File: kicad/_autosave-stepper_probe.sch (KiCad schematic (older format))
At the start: 49 parts, among them J1 Conn_01x04_Male, J2 Conn_01x04_Male, J3 BAT, J4 Serial Port, J5 SWD, J6 Reset header, M1 Motor, Q1 PJA3439, SW1 SW_Push, U1 CC6920BSO-5A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

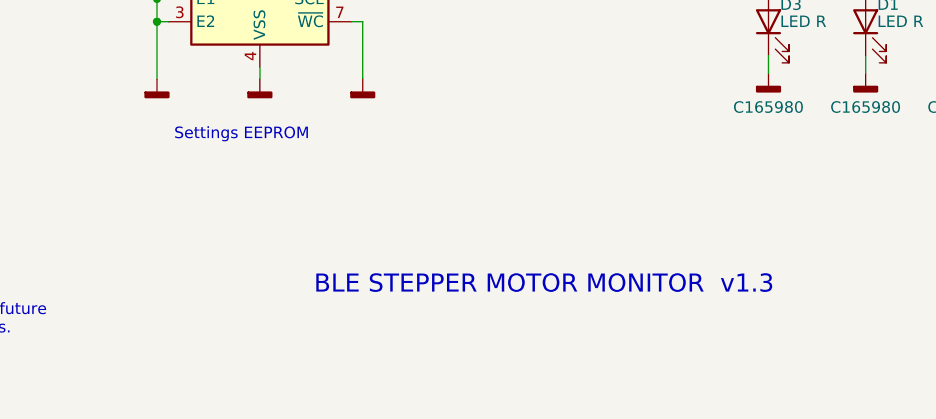
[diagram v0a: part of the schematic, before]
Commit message: Minor PCB tweaks, moved LEDs, added pin 1 marks, added zenner silk screen.  No electrical or bom change.
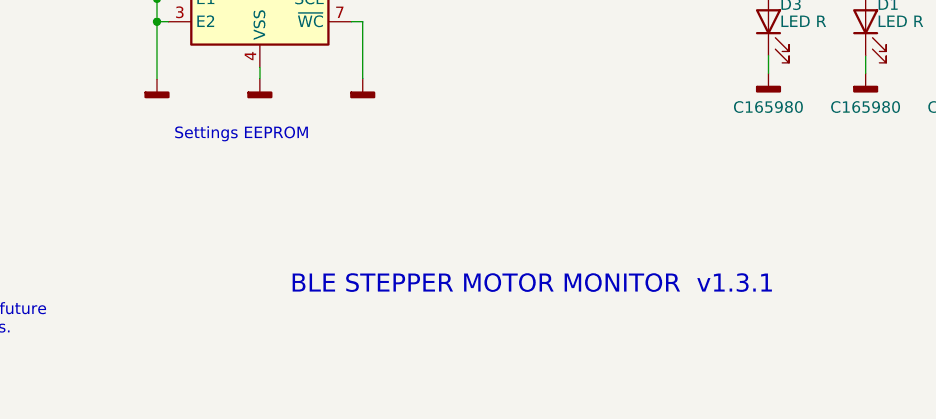
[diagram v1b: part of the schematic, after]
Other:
- note added: "BLE STEPPER MOTOR MONITOR v1.3.1"
- note removed: "BLE STEPPER MOTOR MONITOR v1.3"
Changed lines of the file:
@@
 $EndComp
 Text Notes 9225 6900 2    79   ~ 0
-BLE STEPPER MOTOR MONITOR  v1.3
+BLE STEPPER MOTOR MONITOR  v1.3.1
 $Comp
 L Connector_Generic:Conn_02x05_Odd_Even J5
